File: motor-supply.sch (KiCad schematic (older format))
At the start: 16 parts, among them Q9 2N7002, U2 A8498

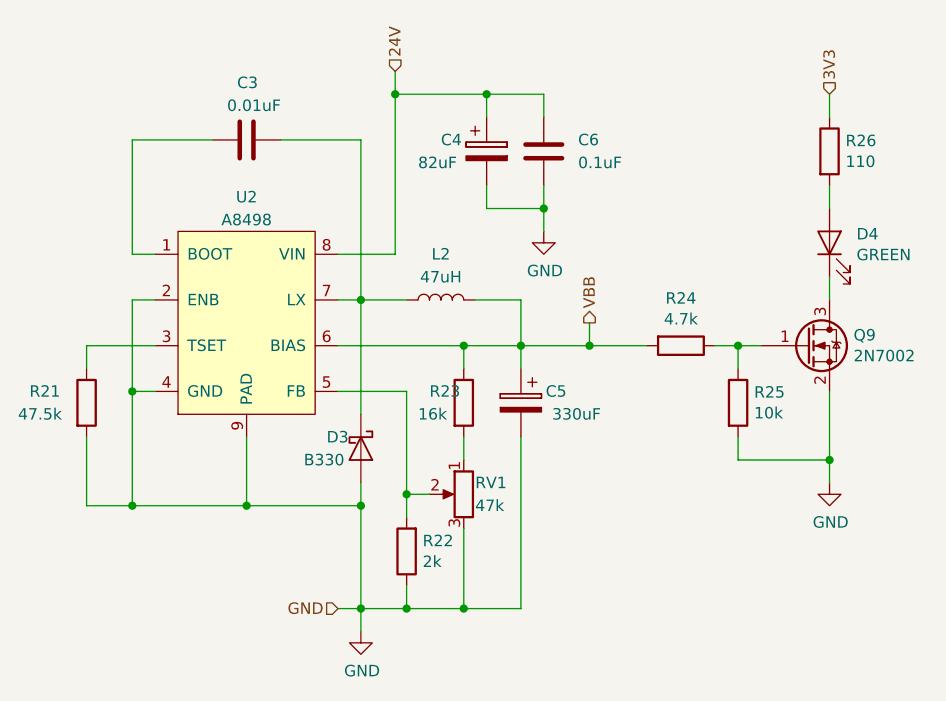
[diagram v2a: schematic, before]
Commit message: PCB creation, improvements of power supply section
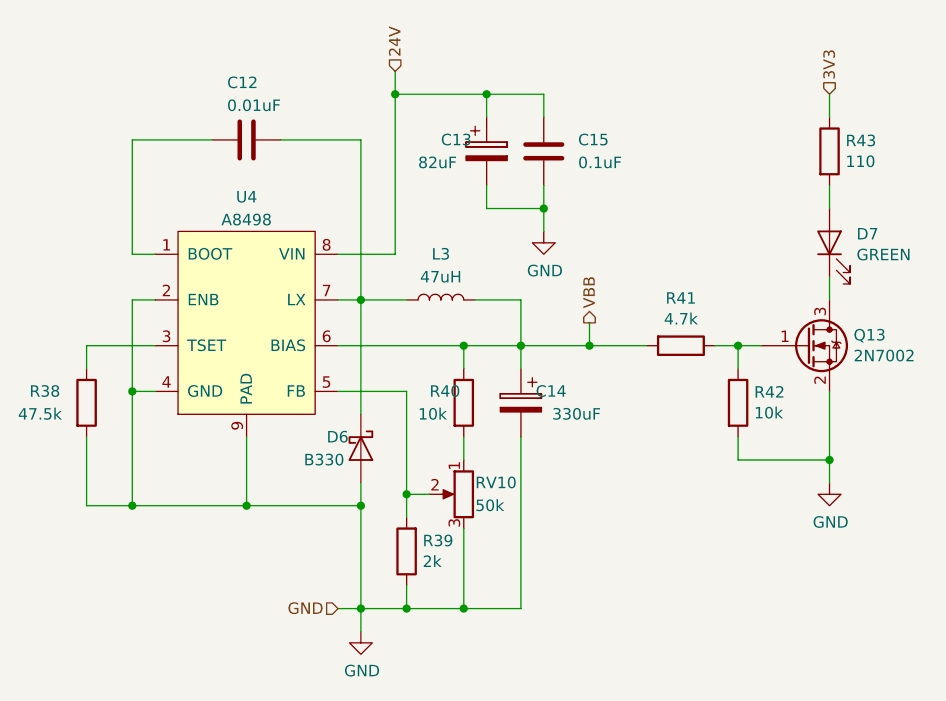
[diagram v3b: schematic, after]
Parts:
- R23: value 16k -> 10k
- R24: footprint Resistor_SMD:R_1206_3216Metric_Pad1.42x1.75mm_HandSolder -> Resistor_SMD:R_0805_2012Metric_Pad1.15x1.40mm_HandSolder
- RV1: value 47k -> 50k; footprint Potentiometer_THT:Potentiometer_Bourns_3386P_Vertical -> Potentiometer_THT:Potentiometer_Bourns_3296Y_Vertical
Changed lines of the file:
@@
 $Descr A4 11693 8268
 encoding utf-8
-Sheet 4 10
+Sheet 8 10
 Title ""
 Date ""
@@
 AR Path="/5BF2FCC4/5BDBDBC7" Ref="R?"  Part="1"
 AR Path="/5C015BBF/5BDBDBC7" Ref="R39"  Part="1"
-F 0 "R22" H 5580 4604 50  0000 R CNN
+F 0 "R39" H 5580 4604 50  0000 R CNN
 F 1 "2k" H 5580 4695 50  0000 R CNN
 F 2 "Resistor_SMD:R_0805_2012Metric_Pad1.15x1.40mm_HandSolder" V 5580 4650 50  0001 C CNN
@@
 AR Path="/5BF2FCC4/5BDBDBCE" Ref="R?"  Part="1"
 AR Path="/5C015BBF/5BDBDBCE" Ref="R40"  Part="1"
-F 0 "R23" H 5750 4050 50  0000 L CNN
-F 1 "16k" H 5700 3950 50  0000 L CNN
+F 0 "R40" H 5750 4050 50  0000 L CNN
+F 1 "10k" H 5700 3950 50  0000 L CNN
 F 2 "Resistor_SMD:R_0805_2012Metric_Pad1.15x1.40mm_HandSolder" V 5830 4000 50  0001 C CNN
 F 3 "~" H 5900 4000 50  0001 C CNN
@@
 AR Path="/5BF2FCC4/5BDBDBD5" Ref="C?"  Part="1"
 AR Path="/5C015BBF/5BDBDBD5" Ref="C15"  Part="1"
-F 0 "C6" H 6100 2850 50  0000 R CNN
+F 0 "C15" H 6100 2850 50  0000 R CNN
 F 1 "0.1uF" H 6100 2950 50  0000 R CNN
 F 2 "Capacitor_SMD:C_0805_2012Metric_Pad1.15x1.40mm_HandSolder" H 6288 2750 50  0001 C CNN
@@
 AR Path="/5BF2FCC4/5BDBDBDC" Ref="C?"  Part="1"
 AR Path="/5C015BBF/5BDBDBDC" Ref="C12"  Part="1"
-F 0 "C3" V 5200 2800 50  0000 L CNN
+F 0 "C12" V 5200 2800 50  0000 L CNN
 F 1 "0.01uF" V 5100 2700 50  0000 L CNN
 F 2 "Capacitor_SMD:C_0603_1608Metric_Pad1.05x0.95mm_HandSolder" H 4988 2700 50  0001 C CNN
@@
 AR Path="/5BF2FCC4/5BDBDBE3" Ref="C?"  Part="1"
 AR Path="/5C015BBF/5BDBDBE3" Ref="C14"  Part="1"
-F 0 "C5" H 5950 4050 50  0000 L CNN
+F 0 "C14" H 5950 4050 50  0000 L CNN
 F 1 "330uF" H 5800 3950 50  0000 L CNN
 F 2 "Capacitor_SMD:CP_Elec_6.3x7.7" H 6188 3850 50  0001 C CNN
@@
 AR Path="/5BF2FCC4/5BDBDBEB" Ref="L?"  Part="1"
 AR Path="/5C015BBF/5BDBDBEB" Ref="L3"  Part="1"
-F 0 "L2" V 6000 3550 50  0000 C CNN
+F 0 "L3" V 6000 3550 50  0000 C CNN
 F 1 "47uH" V 5900 3550 50  0000 C CNN
 F 2 "Inductor_SMD:L_Bourns_SRP1245A" H 5800 3550 50  0001 C CNN
@@
 AR Path="/5BF2FCC4/5BDBDBF2" Ref="RV?"  Part="1"
 AR Path="/5C015BBF/5BDBDBF2" Ref="RV10"  Part="1"
-F 0 "RV1" H 5850 4450 50  0000 R CNN
-F 1 "47k" H 5850 4350 50  0000 R CNN
-F 2 "Potentiometer_THT:Potentiometer_Bourns_3386P_Vertical" H 5900 4400 50  0001 C CNN
+F 0 "RV10" H 5850 4450 50  0000 R CNN
+F 1 "50k" H 5850 4350 50  0000 R CNN
+F 2 "Potentiometer_THT:Potentiometer_Bourns_3296Y_Vertical" H 5900 4400 50  0001 C CNN
 F 3 "~" H 5900 4400 50  0001 C CNN
 	1    5900 4400
@@
 AR Path="/5BF2FCC4/5BDBDBF9" Ref="U?"  Part="1"
 AR Path="/5C015BBF/5BDBDBF9" Ref="U4"  Part="1"
-F 0 "U2" H 4950 4800 50  0000 C CNN
+F 0 "U4" H 4950 4800 50  0000 C CNN
 F 1 "A8498" H 4950 4700 50  0000 C CNN
 F 2 "Package_SO:SOIC-8-1EP_3.9x4.9mm_P1.27mm_EP2.35x2.35mm" H 4800 3950 50  0001 C CNN
@@
 AR Path="/5BF2FCC4/5BDBDC38" Ref="C?"  Part="1"
 AR Path="/5C015BBF/5BDBDC38" Ref="C13"  Part="1"
-F 0 "C4" H 5800 2950 50  0000 L CNN
+F 0 "C13" H 5800 2950 50  0000 L CNN
 F 1 "82uF" H 5700 2850 50  0000 L CNN
 F 2 "Capacitor_SMD:CP_Elec_6.3x5.8" H 6038 2750 50  0001 C CNN
@@
 AR Path="/5BF2FCC4/5BDBDC4C" Ref="R?"  Part="1"
 AR Path="/5C015BBF/5BDBDC4C" Ref="R38"  Part="1"
-F 0 "R21" H 4000 4050 50  0000 L CNN
+F 0 "R38" H 4000 4050 50  0000 L CNN
 F 1 "47.5k" H 3950 3950 50  0000 L CNN
 F 2 "Resistor_SMD:R_0805_2012Metric_Pad1.15x1.40mm_HandSolder" V 4180 4000 50  0001 C CNN
@@
 AR Path="/5BF2FCC4/5BDBDC5F" Ref="Q?"  Part="1"
 AR Path="/5C015BBF/5BDBDC5F" Ref="Q13"  Part="1"
-F 0 "Q9" H 7605 3796 50  0000 L CNN
+F 0 "Q13" H 7605 3796 50  0000 L CNN
 F 1 "2N7002" H 7605 3705 50  0000 L CNN
 F 2 "Package_TO_SOT_SMD:SOT-23_Handsoldering" H 7600 3675 50  0001 L CIN
@@
 AR Path="/5BF2FCC4/5BDBDC66" Ref="R?"  Part="1"
 AR Path="/5C015BBF/5BDBDC66" Ref="R41"  Part="1"
-F 0 "R24" V 6643 3750 50  0000 C CNN
+F 0 "R41" V 6643 3750 50  0000 C CNN
 F 1 "4.7k" V 6734 3750 50  0000 C CNN
-F 2 "Resistor_SMD:R_1206_3216Metric_Pad1.42x1.75mm_HandSolder" V 6780 3750 50  0001 C CNN
+F 2 "Resistor_SMD:R_0805_2012Metric_Pad1.15x1.40mm_HandSolder" V 6780 3750 50  0001 C CNN
 F 3 "~" H 6850 3750 50  0001 C CNN
 	1    6850 3750
@@
 AR Path="/5BF2FCC4/5BDBDC75" Ref="D?"  Part="1"
 AR Path="/5C015BBF/5BDBDC75" Ref="D7"  Part="1"
-F 0 "D4" V 7538 3182 50  0000 R CNN
+F 0 "D7" V 7538 3182 50  0000 R CNN
 F 1 "GREEN" V 7447 3182 50  0000 R CNN
 F 2 "LED_SMD:LED_0603_1608Metric_Pad1.05x0.95mm_HandSolder" H 7500 3300 50  0001 C CNN
@@
 AR Path="/5BF2FCC4/5BDBDC7D" Ref="R?"  Part="1"
 AR Path="/5C015BBF/5BDBDC7D" Ref="R43"  Part="1"
-F 0 "R26" H 7570 2946 50  0000 L CNN
+F 0 "R43" H 7570 2946 50  0000 L CNN
 F 1 "110" H 7570 2855 50  0000 L CNN
 F 2 "Resistor_SMD:R_0805_2012Metric_Pad1.15x1.40mm_HandSolder" V 7430 2900 50  0001 C CNN
@@
 AR Path="/5BF2FCC4/5BDBDC88" Ref="R?"  Part="1"
 AR Path="/5C015BBF/5BDBDC88" Ref="R42"  Part="1"
-F 0 "R25" H 7170 4046 50  0000 L CNN
+F 0 "R42" H 7170 4046 50  0000 L CNN
 F 1 "10k" H 7170 3955 50  0000 L CNN
 F 2 "Resistor_SMD:R_0805_2012Metric_Pad1.15x1.40mm_HandSolder" V 7030 4000 50  0001 C CNN
@@
 AR Path="/5BF2FCC4/5BDBDCA0" Ref="D?"  Part="1"
 AR Path="/5C015BBF/5BDBDCA0" Ref="D6"  Part="1"
-F 0 "D3" V 5400 4050 50  0000 L CNN
+F 0 "D6" V 5400 4050 50  0000 L CNN
 F 1 "B330" V 5500 3950 50  0000 L CNN
 F 2 "Diode_SMD:D_SMA" H 5450 4200 50  0001 C CNN

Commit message: Further work at PCB
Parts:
- R21, R22, R23, R24, R25, R26: footprint Resistor_SMD:R_0805_2012Metric_Pad1.15x1.40mm_HandSolder -> Resistor_SMD:R_0603_1608Metric_Pad1.05x0.95mm_HandSolder
- RV1: footprint Potentiometer_THT:Potentiometer_Bourns_3296Y_Vertical -> Potentiometer_THT:Potentiometer_Vishay_T73XX_Horizontal
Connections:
- net GND: no longer RV1.3
- net at R22.2, U2.5 (FB): now also RV1.3; no longer RV1.2
- net at R23.2: now also RV1.2; no longer RV1.1
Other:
- moved on the sheet: RV1
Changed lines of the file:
@@
 $Descr A4 11693 8268
 encoding utf-8
-Sheet 8 10
+Sheet 4 10
 Title ""
 Date ""
@@
 AR Path="/5BF2FCC4/5BDBDBC7" Ref="R?"  Part="1"
 AR Path="/5C015BBF/5BDBDBC7" Ref="R39"  Part="1"
-F 0 "R39" H 5580 4604 50  0000 R CNN
+F 0 "R22" H 5580 4604 50  0000 R CNN
 F 1 "2k" H 5580 4695 50  0000 R CNN
-F 2 "Resistor_SMD:R_0805_2012Metric_Pad1.15x1.40mm_HandSolder" V 5580 4650 50  0001 C CNN
+F 2 "Resistor_SMD:R_0603_1608Metric_Pad1.05x0.95mm_HandSolder" V 5580 4650 50  0001 C CNN
 F 3 "~" H 5650 4650 50  0001 C CNN
 	1    5650 4650
@@
 AR Path="/5BF2FCC4/5BDBDBCE" Ref="R?"  Part="1"
 AR Path="/5C015BBF/5BDBDBCE" Ref="R40"  Part="1"
-F 0 "R40" H 5750 4050 50  0000 L CNN
+F 0 "R23" H 5750 4050 50  0000 L CNN
 F 1 "10k" H 5700 3950 50  0000 L CNN
-F 2 "Resistor_SMD:R_0805_2012Metric_Pad1.15x1.40mm_HandSolder" V 5830 4000 50  0001 C CNN
+F 2 "Resistor_SMD:R_0603_1608Metric_Pad1.05x0.95mm_HandSolder" V 5830 4000 50  0001 C CNN
 F 3 "~" H 5900 4000 50  0001 C CNN
 	1    5900 4000
@@
 AR Path="/5BF2FCC4/5BDBDBD5" Ref="C?"  Part="1"
 AR Path="/5C015BBF/5BDBDBD5" Ref="C15"  Part="1"
-F 0 "C15" H 6100 2850 50  0000 R CNN
+F 0 "C6" H 6100 2850 50  0000 R CNN
 F 1 "0.1uF" H 6100 2950 50  0000 R CNN
 F 2 "Capacitor_SMD:C_0805_2012Metric_Pad1.15x1.40mm_HandSolder" H 6288 2750 50  0001 C CNN
@@
 AR Path="/5BF2FCC4/5BDBDBDC" Ref="C?"  Part="1"
 AR Path="/5C015BBF/5BDBDBDC" Ref="C12"  Part="1"
-F 0 "C12" V 5200 2800 50  0000 L CNN
+F 0 "C3" V 5200 2800 50  0000 L CNN
 F 1 "0.01uF" V 5100 2700 50  0000 L CNN
 F 2 "Capacitor_SMD:C_0603_1608Metric_Pad1.05x0.95mm_HandSolder" H 4988 2700 50  0001 C CNN
@@
 AR Path="/5BF2FCC4/5BDBDBE3" Ref="C?"  Part="1"
 AR Path="/5C015BBF/5BDBDBE3" Ref="C14"  Part="1"
-F 0 "C14" H 5950 4050 50  0000 L CNN
+F 0 "C5" H 5950 4050 50  0000 L CNN
 F 1 "330uF" H 5800 3950 50  0000 L CNN
 F 2 "Capacitor_SMD:CP_Elec_6.3x7.7" H 6188 3850 50  0001 C CNN
@@
 AR Path="/5BF2FCC4/5BDBDBEB" Ref="L?"  Part="1"
 AR Path="/5C015BBF/5BDBDBEB" Ref="L3"  Part="1"
-F 0 "L3" V 6000 3550 50  0000 C CNN
+F 0 "L2" V 6000 3550 50  0000 C CNN
 F 1 "47uH" V 5900 3550 50  0000 C CNN
 F 2 "Inductor_SMD:L_Bourns_SRP1245A" H 5800 3550 50  0001 C CNN
@@
 AR Path="/5BF2FCC4/5BDBDBF2" Ref="RV?"  Part="1"
 AR Path="/5C015BBF/5BDBDBF2" Ref="RV10"  Part="1"
-F 0 "RV10" H 5850 4450 50  0000 R CNN
+F 0 "RV1" H 5850 4450 50  0000 R CNN
 F 1 "50k" H 5850 4350 50  0000 R CNN
-F 2 "Potentiometer_THT:Potentiometer_Bourns_3296Y_Vertical" H 5900 4400 50  0001 C CNN
+F 2 "Potentiometer_THT:Potentiometer_Vishay_T73XX_Horizontal" H 5900 4400 50  0001 C CNN
 F 3 "~" H 5900 4400 50  0001 C CNN
 	1    5900 4400
-	-1   0    0    -1
+	0    1    -1   0
 $EndComp
 $Comp
@@
 AR Path="/5BF2FCC4/5BDBDBF9" Ref="U?"  Part="1"
 AR Path="/5C015BBF/5BDBDBF9" Ref="U4"  Part="1"
-F 0 "U4" H 4950 4800 50  0000 C CNN
+F 0 "U2" H 4950 4800 50  0000 C CNN
 F 1 "A8498" H 4950 4700 50  0000 C CNN
 F 2 "Package_SO:SOIC-8-1EP_3.9x4.9mm_P1.27mm_EP2.35x2.35mm" H 4800 3950 50  0001 C CNN
@@
 AR Path="/5BF2FCC4/5BDBDC17" Ref="#PWR?"  Part="1"
 AR Path="/5C015BBF/5BDBDC17" Ref="#PWR012"  Part="1"
-F 0 "#PWR012" H 6250 3000 50  0001 C CNN
+F 0 "#PWR06" H 6250 3000 50  0001 C CNN
 F 1 "GND" H 6255 3077 50  0000 C CNN
 F 2 "" H 6250 3250 50  0001 C CNN
@@
 AR Path="/5BF2FCC4/5BDBDC1D" Ref="#PWR?"  Part="1"
 AR Path="/5C015BBF/5BDBDC1D" Ref="#PWR011"  Part="1"
-F 0 "#PWR011" H 5450 4750 50  0001 C CNN
+F 0 "#PWR05" H 5450 4750 50  0001 C CNN
 F 1 "GND" H 5455 4827 50  0000 C CNN
 F 2 "" H 5450 5000 50  0001 C CNN
@@
 Wire Wire Line
 	5450 4900 5450 4450
-Wire Wire Line
-	5650 4900 5900 4900
-Wire Wire Line
-	5900 4900 5900 4550
 Connection ~ 5650 4900
 Wire Wire Line
-	5900 4900 6150 4900
-Wire Wire Line
 	6150 4900 6150 4150
-Connection ~ 5900 4900
 Wire Wire Line
 	4950 4150 4950 4450
@@
 AR Path="/5BF2FCC4/5BDBDC38" Ref="C?"  Part="1"
 AR Path="/5C015BBF/5BDBDC38" Ref="C13"  Part="1"
-F 0 "C13" H 5800 2950 50  0000 L CNN
+F 0 "C4" H 5800 2950 50  0000 L CNN
 F 1 "82uF" H 5700 2850 50  0000 L CNN
 F 2 "Capacitor_SMD:CP_Elec_6.3x5.8" H 6038 2750 50  0001 C CNN
@@
 AR Path="/5BF2FCC4/5BDBDC4C" Ref="R?"  Part="1"
 AR Path="/5C015BBF/5BDBDC4C" Ref="R38"  Part="1"
-F 0 "R38" H 4000 4050 50  0000 L CNN
+F 0 "R21" H 4000 4050 50  0000 L CNN
 F 1 "47.5k" H 3950 3950 50  0000 L CNN
-F 2 "Resistor_SMD:R_0805_2012Metric_Pad1.15x1.40mm_HandSolder" V 4180 4000 50  0001 C CNN
+F 2 "Resistor_SMD:R_0603_1608Metric_Pad1.05x0.95mm_HandSolder" V 4180 4000 50  0001 C CNN
 F 3 "~" H 4250 4000 50  0001 C CNN
 	1    4250 4000
@@
 AR Path="/5BF2FCC4/5BDBDC5F" Ref="Q?"  Part="1"
 AR Path="/5C015BBF/5BDBDC5F" Ref="Q13"  Part="1"
-F 0 "Q13" H 7605 3796 50  0000 L CNN
+F 0 "Q9" H 7605 3796 50  0000 L CNN
 F 1 "2N7002" H 7605 3705 50  0000 L CNN
 F 2 "Package_TO_SOT_SMD:SOT-23_Handsoldering" H 7600 3675 50  0001 L CIN
@@
 AR Path="/5BF2FCC4/5BDBDC66" Ref="R?"  Part="1"
 AR Path="/5C015BBF/5BDBDC66" Ref="R41"  Part="1"
-F 0 "R41" V 6643 3750 50  0000 C CNN
+F 0 "R24" V 6643 3750 50  0000 C CNN
 F 1 "4.7k" V 6734 3750 50  0000 C CNN
-F 2 "Resistor_SMD:R_0805_2012Metric_Pad1.15x1.40mm_HandSolder" V 6780 3750 50  0001 C CNN
+F 2 "Resistor_SMD:R_0603_1608Metric_Pad1.05x0.95mm_HandSolder" V 6780 3750 50  0001 C CNN
 F 3 "~" H 6850 3750 50  0001 C CNN
 	1    6850 3750
@@
 AR Path="/5BF2FCC4/5BDBDC6D" Ref="#PWR?"  Part="1"
 AR Path="/5C015BBF/5BDBDC6D" Ref="#PWR013"  Part="1"
-F 0 "#PWR013" H 7500 4100 50  0001 C CNN
+F 0 "#PWR07" H 7500 4100 50  0001 C CNN
 F 1 "GND" H 7505 4177 50  0000 C CNN
 F 2 "" H 7500 4350 50  0001 C CNN
@@
 AR Path="/5BF2FCC4/5BDBDC75" Ref="D?"  Part="1"
 AR Path="/5C015BBF/5BDBDC75" Ref="D7"  Part="1"
-F 0 "D7" V 7538 3182 50  0000 R CNN
+F 0 "D4" V 7538 3182 50  0000 R CNN
 F 1 "GREEN" V 7447 3182 50  0000 R CNN
 F 2 "LED_SMD:LED_0603_1608Metric_Pad1.05x0.95mm_HandSolder" H 7500 3300 50  0001 C CNN
@@
 AR Path="/5BF2FCC4/5BDBDC7D" Ref="R?"  Part="1"
 AR Path="/5C015BBF/5BDBDC7D" Ref="R43"  Part="1"
-F 0 "R43" H 7570 2946 50  0000 L CNN
+F 0 "R26" H 7570 2946 50  0000 L CNN
 F 1 "110" H 7570 2855 50  0000 L CNN
-F 2 "Resistor_SMD:R_0805_2012Metric_Pad1.15x1.40mm_HandSolder" V 7430 2900 50  0001 C CNN
+F 2 "Resistor_SMD:R_0603_1608Metric_Pad1.05x0.95mm_HandSolder" V 7430 2900 50  0001 C CNN
 F 3 "~" H 7500 2900 50  0001 C CNN
 	1    7500 2900
@@
 AR Path="/5BF2FCC4/5BDBDC88" Ref="R?"  Part="1"
 AR Path="/5C015BBF/5BDBDC88" Ref="R42"  Part="1"
-F 0 "R42" H 7170 4046 50  0000 L CNN
+F 0 "R25" H 7170 4046 50  0000 L CNN
 F 1 "10k" H 7170 3955 50  0000 L CNN
-F 2 "Resistor_SMD:R_0805_2012Metric_Pad1.15x1.40mm_HandSolder" V 7030 4000 50  0001 C CNN
+F 2 "Resistor_SMD:R_0603_1608Metric_Pad1.05x0.95mm_HandSolder" V 7030 4000 50  0001 C CNN
 F 3 "~" H 7100 4000 50  0001 C CNN
 	1    7100 4000
@@
 AR Path="/5BF2FCC4/5BDBDCA0" Ref="D?"  Part="1"
 AR Path="/5C015BBF/5BDBDCA0" Ref="D6"  Part="1"
-F 0 "D6" V 5400 4050 50  0000 L CNN
+F 0 "D3" V 5400 4050 50  0000 L CNN
 F 1 "B330" V 5500 3950 50  0000 L CNN
 F 2 "Diode_SMD:D_SMA" H 5450 4200 50  0001 C CNN
@@
 	5600 2550 5600 2650
 Connection ~ 5600 2650
+Wire Wire Line
+	5650 4900 6150 4900
 $EndSCHEMATC
